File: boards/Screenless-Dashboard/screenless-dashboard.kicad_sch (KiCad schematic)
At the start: 0 parts

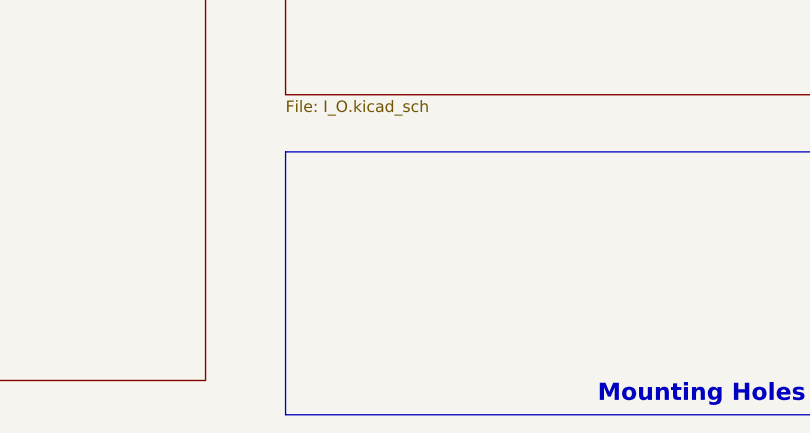
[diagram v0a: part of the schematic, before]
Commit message: add mounting holes
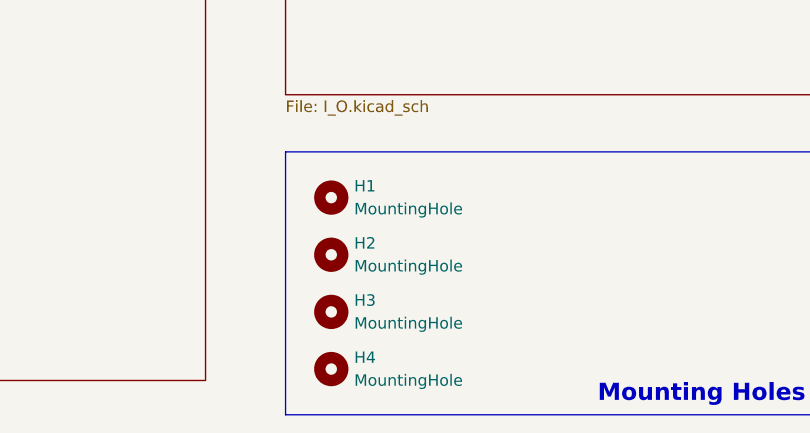
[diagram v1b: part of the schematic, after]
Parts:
- added H1, H2, H3, H4: MountingHole, Module:Maple_Mini, symbol Mechanical:MountingHole
